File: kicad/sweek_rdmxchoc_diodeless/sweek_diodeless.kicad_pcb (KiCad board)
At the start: 2 copper layers, 124.6 x 107.6 mm, 29 parts, among them J1 Conn_01x04_Socket, U1 RP2040_Zero

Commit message: Update kicad sweek diodeless
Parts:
- moved R4 0.29 mm to (119.9, 85.1)
- moved R3 0.26 mm to (119.9, 82.6)
- moved R2 0.09 mm to (119.9, 80.0)
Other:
- board text removed: "Sweek is inspired"
- board text removed: "and ferris designs."
- board text removed: "in the sweep"
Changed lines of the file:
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@@
 			(layer "F.SilkS"
 				(type "Top Silk Screen")
+				(color "White")
 			)
 			(layer "F.Paste"
@@
 			(layer "F.Mask"
 				(type "Top Solder Mask")
+				(color "Black")
 				(thickness 0.01)
 			)
@@
 			(layer "B.Mask"
 				(type "Bottom Solder Mask")
+				(color "Black")
 				(thickness 0.01)
 			)
@@
 			(layer "B.SilkS"
 				(type "Bottom Silk Screen")
+				(color "White")
 			)
 			(copper_finish "None")
@@
 	(footprint "Resistor_SMD:R_1206_3216Metric_Pad1.30x1.75mm_HandSolder"
 		(layer "F.Cu")
-		(at 119.904998 85.405 180)
+		(at 119.905004 85.115001 180)
 		(descr "Resistor SMD 1206 (3216 Metric), square (rectangular) end terminal, IPC-7351 nominal with elongated pad for handsoldering. (Body size source: IPC-SM-782 page 72, https://www.pcb-3d.com/wordpress/wp-content/uploads/ipc-sm-782a_amendment_1_and_2.pdf), generated with kicad-footprint-generator")
 		(tags "resistor handsolder")
@@
 	(footprint "Resistor_SMD:R_1206_3216Metric_Pad1.30x1.75mm_HandSolder"
 		(layer "F.Cu")
-		(at 119.944998 80.125001 180)
+		(at 119.924594 80.035005 180)
 		(descr "Resistor SMD 1206 (3216 Metric), square (rectangular) end terminal, IPC-7351 nominal with elongated pad for handsoldering. (Body size source: IPC-SM-782 page 72, https://www.pcb-3d.com/wordpress/wp-content/uploads/ipc-sm-782a_amendment_1_and_2.pdf), generated with kicad-footprint-generator")
 		(tags "resistor handsolder")
@@
 	(footprint "Resistor_SMD:R_1206_3216Metric_Pad1.30x1.75mm_HandSolder"
 		(layer "F.Cu")
-		(at 119.934996 82.814999 180)
+		(at 119.925004 82.555001 180)
 		(descr "Resistor SMD 1206 (3216 Metric), square (rectangular) end terminal, IPC-7351 nominal with elongated pad for handsoldering. (Body size source: IPC-SM-782 page 72, https://www.pcb-3d.com/wordpress/wp-content/uploads/ipc-sm-782a_amendment_1_and_2.pdf), generated with kicad-footprint-generator")
 		(tags "resistor handsolder")
@@
 		(layer "Edge.Cuts")
 	)
-	(gr_text "Sweek is inspired"
-		(at 92.865 99.545 342)
-		(layer "F.SilkS")
-		(effects
-			(font
-				(size 0.8 0.8)
-				(thickness 0.1)
-			)
-		)
-	)
-	(gr_text "in the sweep "
-		(at 102.565 103.425 335)
-		(layer "F.SilkS")
-		(effects
-			(font
-				(size 0.8 0.8)
-				(thickness 0.1)
-			)
-		)
-	)
-	(gr_text "and ferris designs."
-		(at 111.495 108.295 330)
-		(layer "F.SilkS")
-		(effects
-			(font
-				(size 0.8 0.8)
-				(thickness 0.1)
-			)
-		)
-	)
-	(gr_text "in the sweep "
-		(at 102.198577 103.435422 335)
-		(layer "B.SilkS")
-		(effects
-			(font
-				(size 0.8 0.8)
-				(thickness 0.1)
-			)
-			(justify mirror)
-		)
-	)
-	(gr_text "Sweek is inspired"
-		(at 111.405868 108.372035 328)
-		(layer "B.SilkS")
-		(effects
-			(font
-				(size 0.8 0.8)
-				(thickness 0.1)
-			)
-			(justify mirror)
-		)
-	)
-	(gr_text "and ferris designs."
-		(at 92.727847 99.725019 340)
-		(layer "B.SilkS")
-		(effects
-			(font
-				(size 0.8 0.8)
-				(thickness 0.1)
-			)
-			(justify mirror)
-		)
-	)
 	(segment
 		(start 21.615 42.706314)
@@
 	)
 	(segment
-		(start 123.714999 85.405001)
-		(end 121.455002 85.405001)
+		(start 119.585 32.135)
+		(end 119.025 31.575)
 		(width 0.5)
 		(layer "F.Cu")
@@
 	)
 	(segment
-		(start 126.775 82.345)
-		(end 123.714999 85.405001)
+		(start 124.004998 85.115002)
+		(end 121.455008 85.115002)
 		(width 0.5)
 		(layer "F.Cu")
@@
 	)
 	(segment
-		(start 119.585 32.135)
-		(end 119.025 31.575)
+		(start 119.025 31.575)
+		(end 115.0775 31.575)
 		(width 0.5)
 		(layer "F.Cu")
@@
 	)
 	(segment
-		(start 119.025 31.575)
-		(end 115.0775 31.575)
+		(start 115.0775 31.575)
+		(end 113.55625 30.05375)
 		(width 0.5)
 		(layer "F.Cu")
@@
 	)
 	(segment
-		(start 115.0775 31.575)
-		(end 113.55625 30.05375)
+		(start 126.775 82.345)
+		(end 124.004998 85.115002)
 		(width 0.5)
 		(layer "F.Cu")
@@
 	)
 	(segment
-		(start 125.045 77.105)
-		(end 125.045 78.435)
+		(start 123.024995 80.035005)
+		(end 121.474594 80.035005)
 		(width 0.5)
 		(layer "F.Cu")
@@
 	)
 	(segment
-		(start 125.045 78.435)
-		(end 123.354999 80.125001)
+		(start 125.045 77.105)
+		(end 125.045 78.015)
 		(width 0.5)
 		(layer "F.Cu")
@@
 	)
 	(segment
-		(start 123.354999 80.125001)
-		(end 121.494998 80.125001)
+		(start 125.045 78.015)
+		(end 123.024995 80.035005)
 		(width 0.5)
 		(layer "F.Cu")
@@
 	(segment
 		(start 127.515 78.435)
-		(end 123.135 82.815)
+		(end 123.394998 82.555002)
 		(width 0.5)
 		(layer "F.Cu")
@@
 	)
 	(segment
-		(start 123.135 82.815)
-		(end 121.485 82.815)
+		(start 123.394998 82.555002)
+		(end 121.475008 82.555002)
 		(width 0.5)
 		(layer "F.Cu")

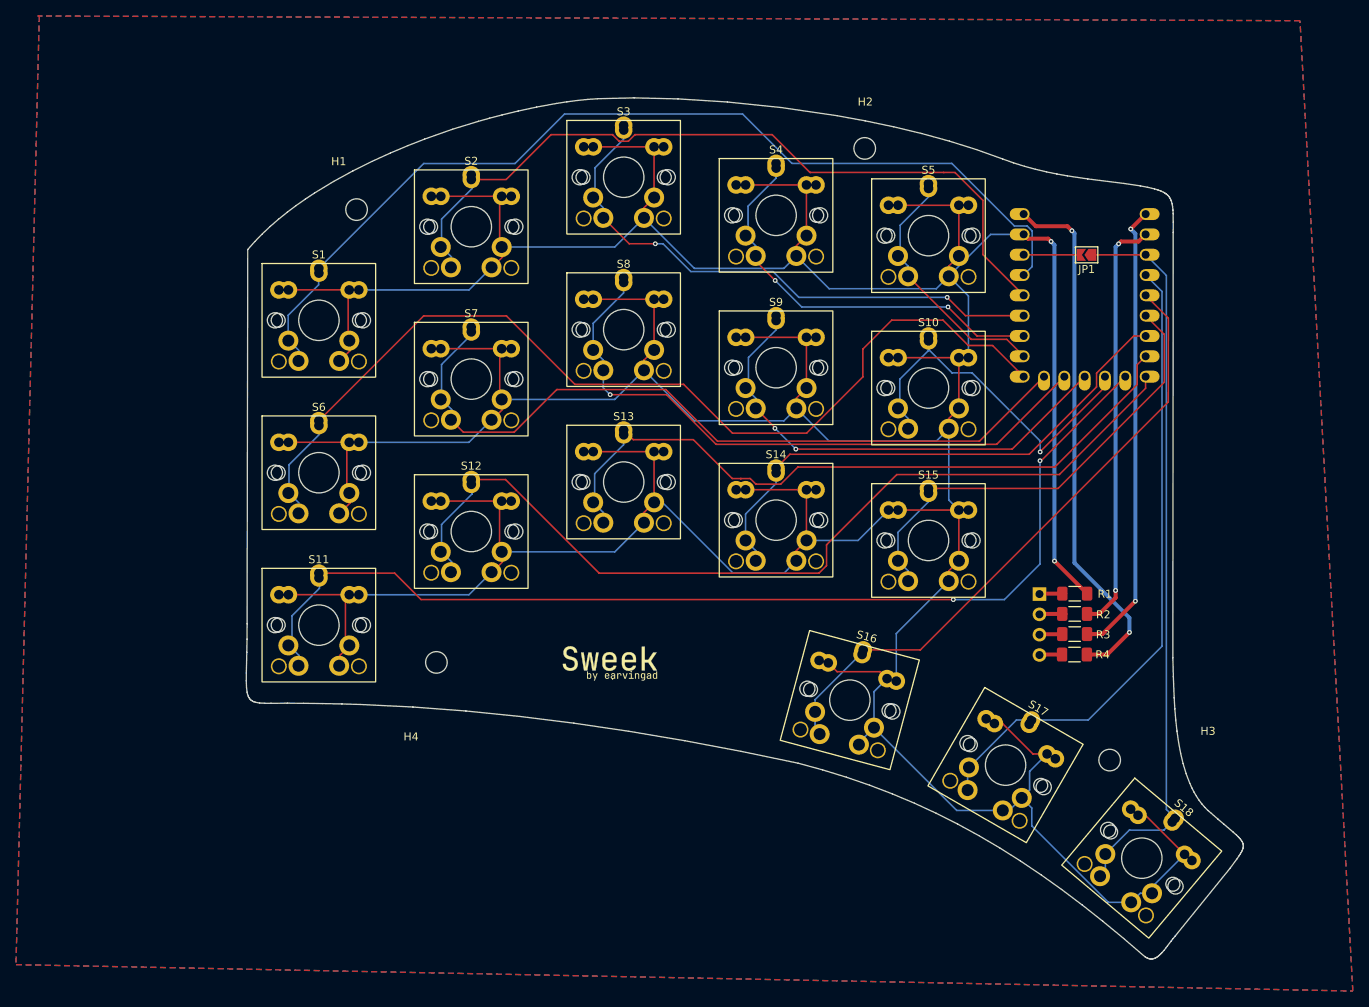
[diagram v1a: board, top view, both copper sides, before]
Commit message: Update diodeless kicad files for v1.0.1
Update diodeless kicad files for v1.0.1
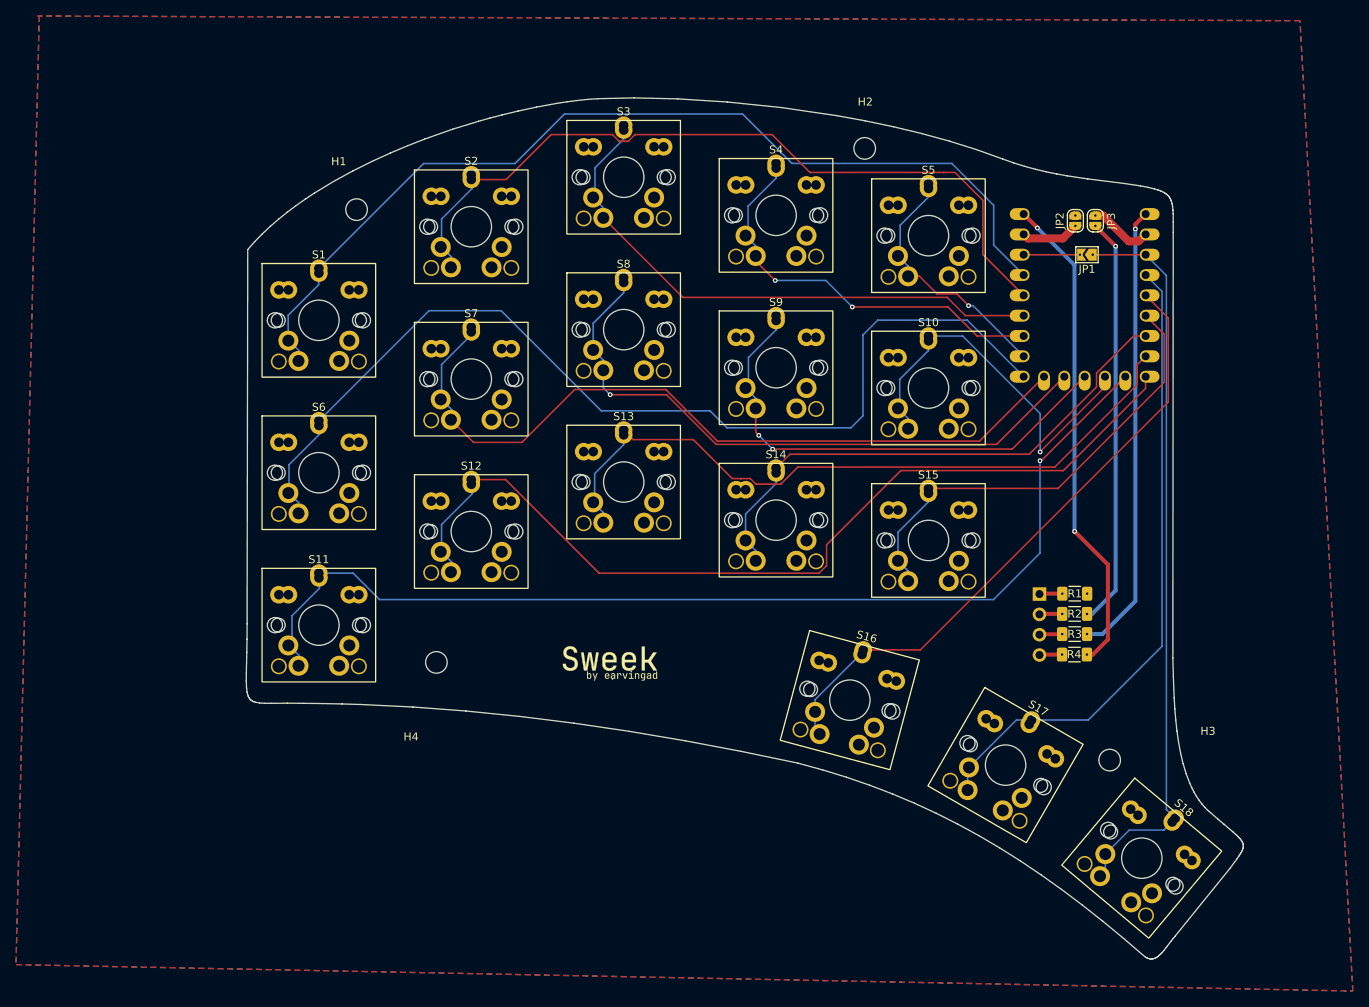
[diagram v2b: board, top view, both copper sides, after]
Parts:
- added JP2: SolderJumper_2_Open, Jumper:SolderJumper-2_P1.3mm_Open_RoundedPad1.0x1.5mm_custom, F.Cu at (120.0, 30.9)
- added JP3: SolderJumper_2_Open, Jumper:SolderJumper-2_P1.3mm_Open_RoundedPad1.0x1.5mm_custom, F.Cu at (122.5, 30.9)
- JP1: footprint Jumper:SolderJumper-2_P1.3mm_Open_TrianglePad1.0x1.5mm -> Jumper:SolderJumper-2_P1.3mm_Open_TrianglePad1.0x1.5mm_custom
- R1, R2, R3, R4: footprint Resistor_SMD:R_1206_3216Metric_Pad1.30x1.75mm_HandSolder -> Resistor_SMD:R_1206_3216Metric_Pad1.30x1.75mm_custom
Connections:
- U1 pad 2: RX -> Net-(JP3-A)
- U1 pad 22: GND -> Net-(JP2-B)
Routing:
- net GND: track 685.4 -> 0.22 mm, vias 2 -> 0
- net Net-(JP3-A): track 0.00 -> 7.98 mm
- net Net-(JP2-B): track 0.00 -> 7.32 mm
- net VCC_5: track 66.5 -> 61.1 mm
- net S6: track 122.8 -> 126.7 mm
- net S1: track 121.0 -> 119.2 mm
- net S9: track 61.4 -> 63.1 mm
- net S10: track 47.6 -> 49.2 mm
- net RX: track 52.7 -> 51.4 mm, vias 2 -> 1
- net S7: track 96.7 -> 97.7 mm
- net S5: track 33.2 -> 32.3 mm, vias 0 -> 1
- net S11: track 135.0 -> 134.2 mm, vias 2 -> 1
- net TX: track 58.6 -> 58.1 mm, vias 2 -> 1
- net S3: vias 2 -> 0
- added copper zone on B.Cu, net GND
- added copper zone on F.Cu, net GND
- removed copper zone on B.Cu, net (none)
- removed copper zone on F.Cu, net (none)
